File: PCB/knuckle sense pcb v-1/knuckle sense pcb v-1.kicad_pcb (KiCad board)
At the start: 2 copper layers, 56.5 x 58 mm, 6 parts

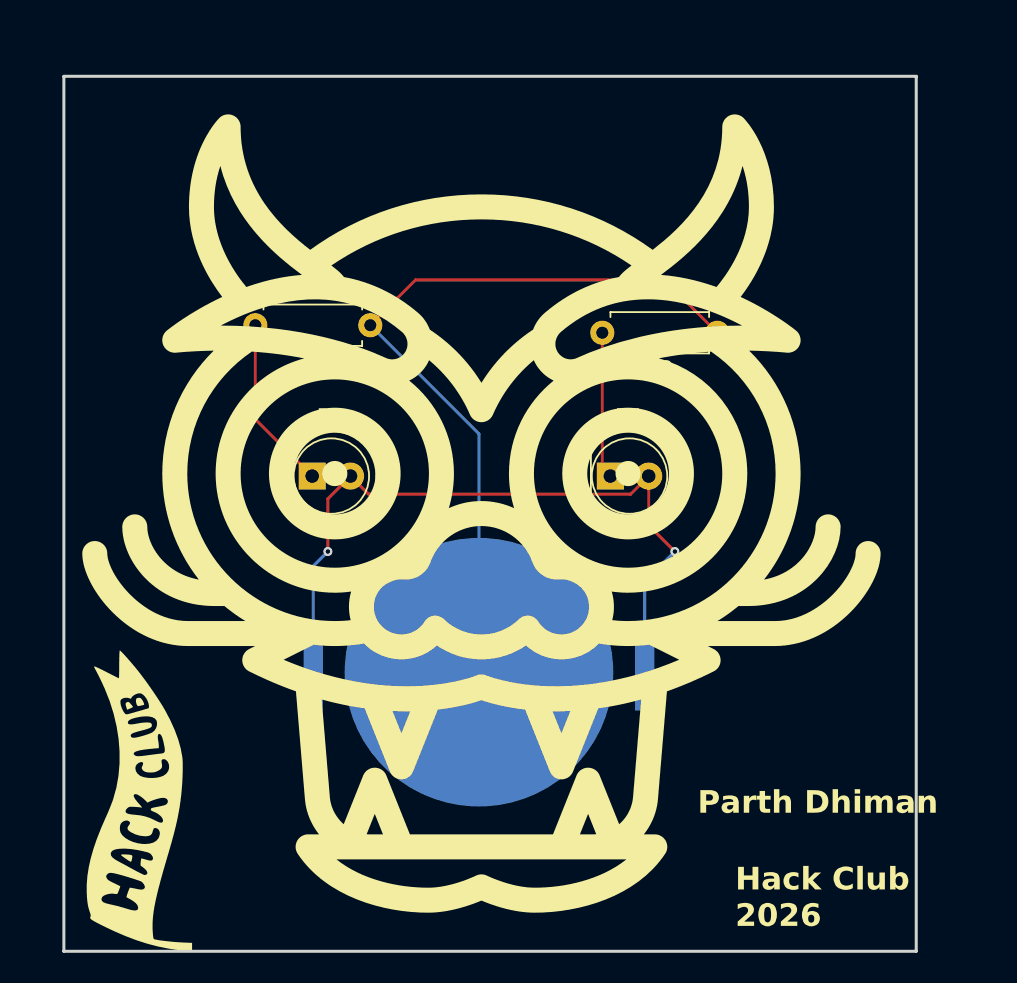
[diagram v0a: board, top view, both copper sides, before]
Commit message: updated pcb edge trace
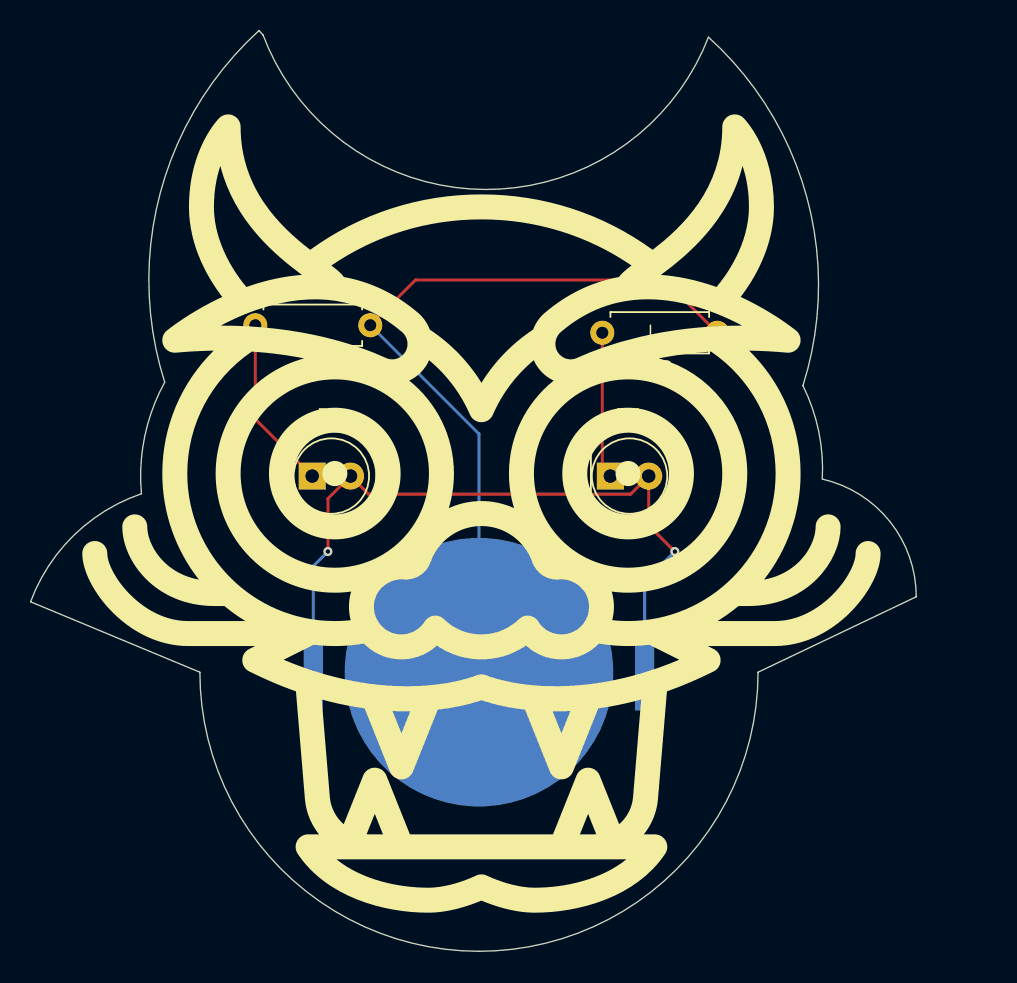
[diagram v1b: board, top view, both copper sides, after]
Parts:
- G***: moved to B.Cu
- moved G*** 41.7 mm to (186.0, 66.0), turned to 180 degrees
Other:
- board size 56.5 x 58 mm -> 58.7 x 61 mm
- board text added: "Hack Club Shenzhen"
- board text removed: "Hack Club 2026"
